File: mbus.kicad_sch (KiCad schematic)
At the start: 30 parts

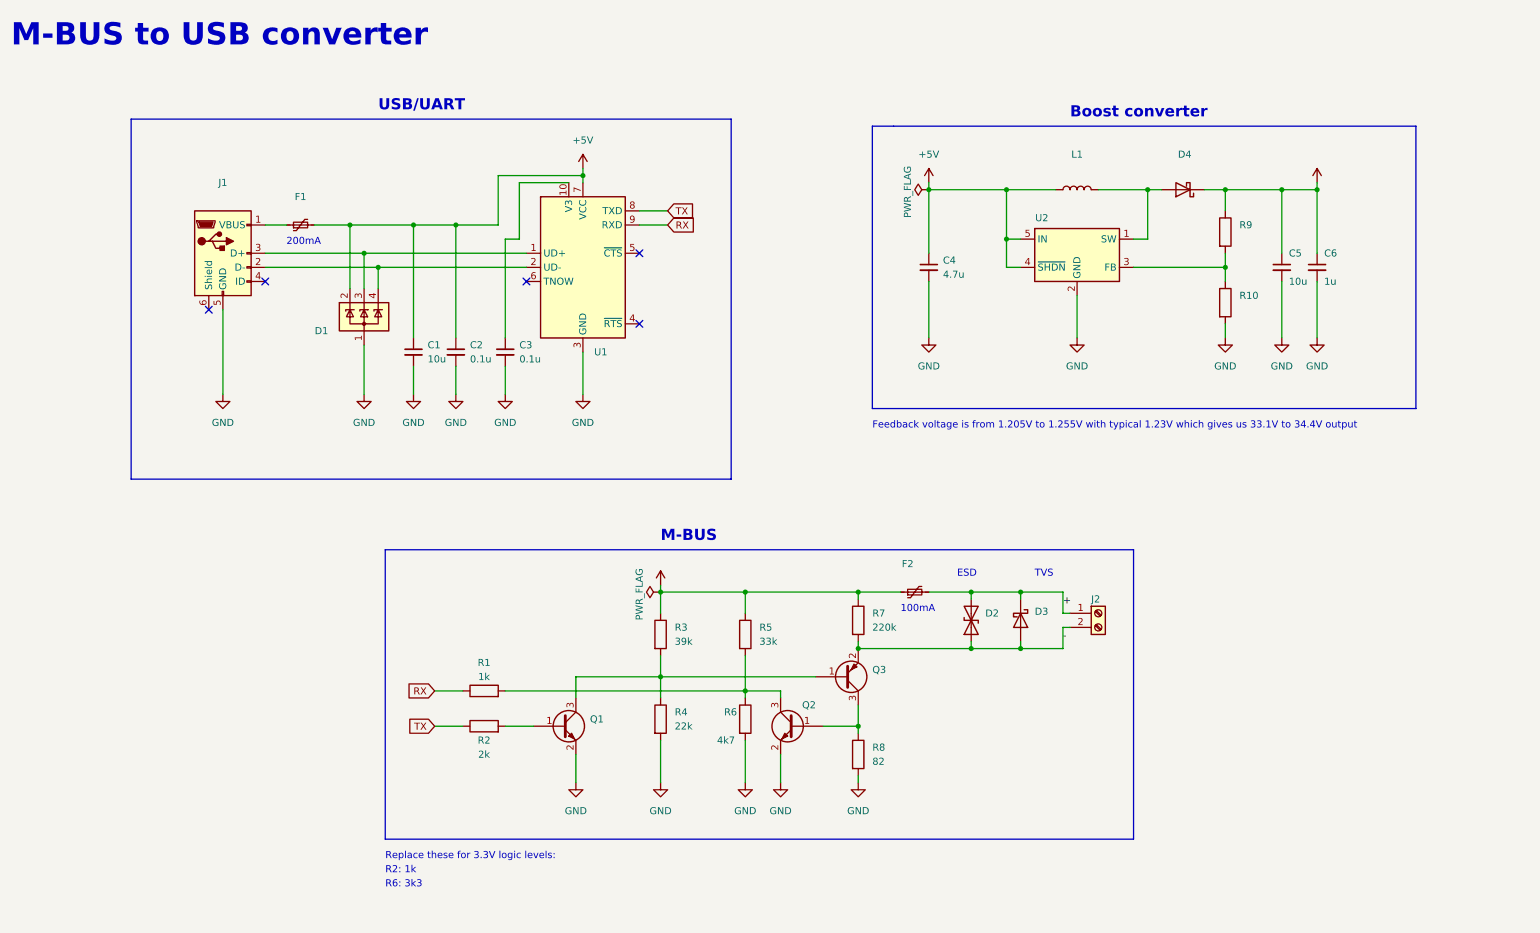
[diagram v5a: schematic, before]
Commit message: Replaced microUSB with type C, changed ESD protection IC
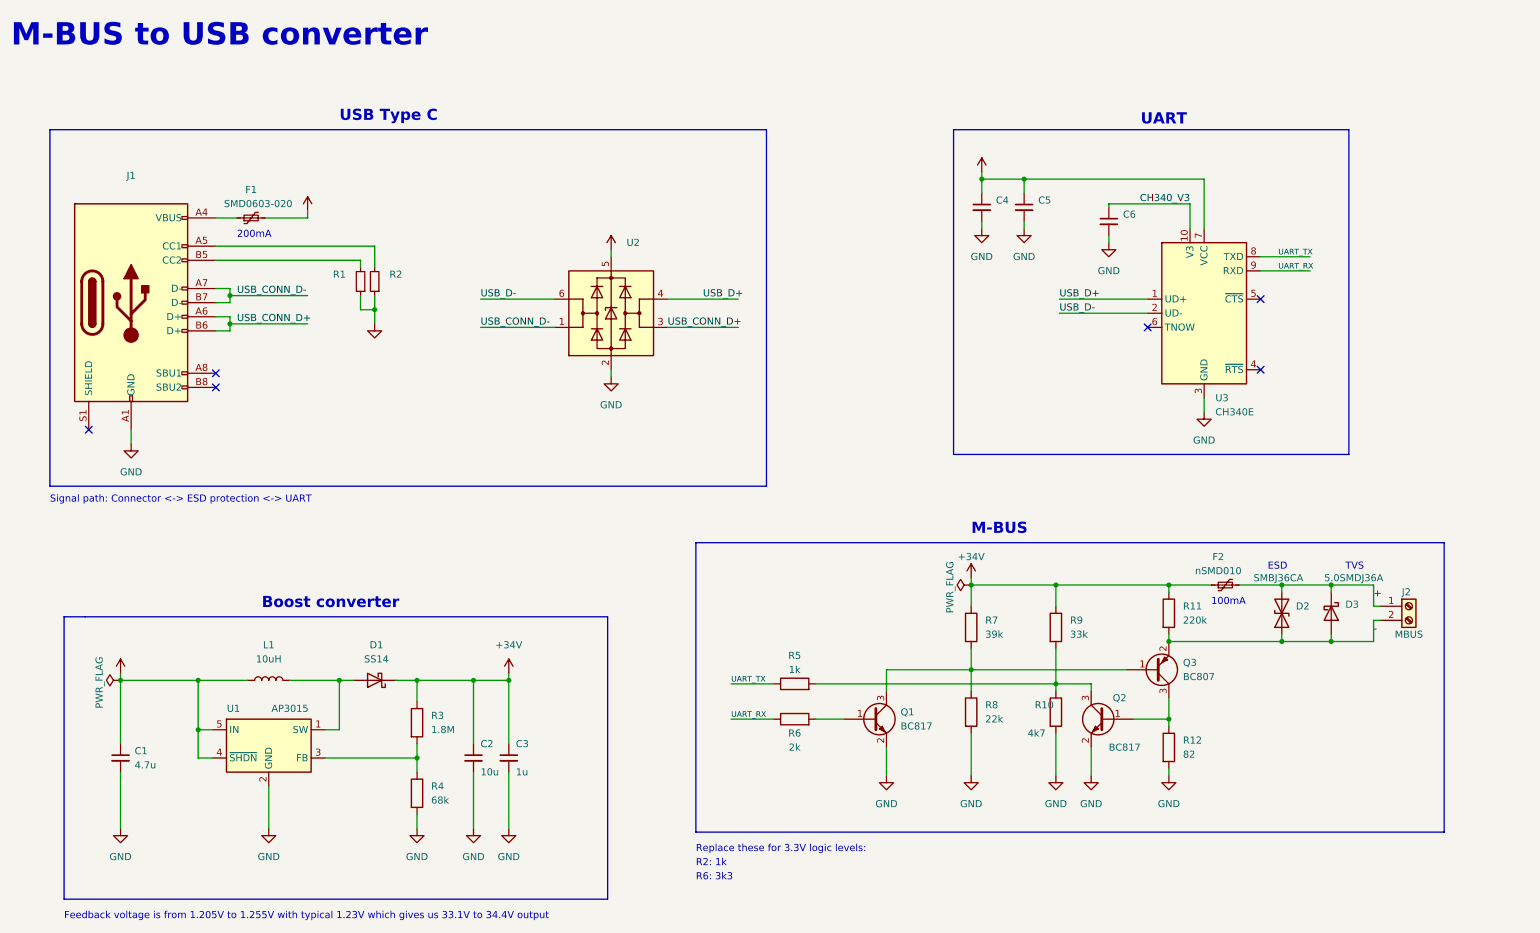
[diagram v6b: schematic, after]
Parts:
- removed D1: (no value), symbol Power_Protection:SP0503BAHT
- removed J1: (no value), symbol Connector:USB_B_Micro
- added J1: (no value), symbol Connector:USB_C_Receptacle_USB2.0
- added R1, R2: (no value), symbol Device:R_Small
- added U2: (no value), symbol Power_Protection:USBLC6-2SC6
- C4: renamed from C1; value 10u -> (none); footprint Capacitor_SMD:C_0603_1608Metric -> (none)
- C5: renamed from C2; value 0.1u -> (none); footprint Capacitor_SMD:C_0603_1608Metric -> (none)
- C6: renamed from C3; value 0.1u -> (none); footprint Capacitor_SMD:C_0603_1608Metric -> (none)
- D1: renamed from D4; value (none) -> SS14; footprint (none) -> Diode_SMD:D_SOD-123F
- D2: value (none) -> SMBJ36CA; footprint (none) -> Diode_SMD:D_SMB
- D3: value (none) -> 5.0SMDJ36A; footprint (none) -> Diode_SMD:D_SMC
- F1: value (none) -> SMD0603-020; footprint (none) -> Fuse:Fuse_0603_1608Metric
- F2: value (none) -> nSMD010; footprint (none) -> Fuse:Fuse_1206_3216Metric
- J2: value (none) -> MBUS; footprint (none) -> TerminalBlock_Phoenix:TerminalBlock_Phoenix_PT-1,5-2-5.0-H_1x02_P5.00mm_Horizontal
- L1: value (none) -> 10uH; footprint (none) -> Inductor_SMD:L_Sunlord_MWSA0518_5.4x5.2mm
- Q1, Q2: value (none) -> BC817; footprint (none) -> Package_TO_SOT_SMD:SOT-23
- Q3: value (none) -> BC807; footprint (none) -> Package_TO_SOT_SMD:SOT-23
- R3: renamed from R9; value (none) -> 1.8M; footprint (none) -> Resistor_SMD:R_0603_1608Metric
- R4: renamed from R10; value (none) -> 68k; footprint (none) -> Resistor_SMD:R_0603_1608Metric
- U1: renamed from U2; value (none) -> AP3015; footprint (none) -> Package_TO_SOT_SMD:SOT-23-5
- U3: renamed from U1; value (none) -> CH340E; footprint (none) -> Package_SO:MSOP-10_3x3mm_P0.5mm
- renumbered C4 to C1, C5 to C2, C6 to C3, R6 to R10, R7 to R11, R8 to R12, R1 to R5, R2 to R6, R3 to R7, R4 to R8, R5 to R9
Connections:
- net GND: now also J1.A1 (GND), J1.A12 (GND), J1.B1 (GND), J1.B12 (GND), R1.1, R2.1, U2.2 (GND)
- net USB_D+: now reaches U3.1 (UD+)
- net USB_D+: now also U2.4 (I/O2)
- net CH340_V3: now reaches C6.1, U3.10 (V3)
- net USB_D-: now reaches U3.2 (UD-)
- net USB_D-: now also U2.6 (I/O1)
- net at F1.1: now also J1.A4 (VBUS), J1.A9 (VBUS), J1.B4 (VBUS), J1.B9 (VBUS)
- net +5V renamed VBUS
- net VBUS: now also U2.5 (VBUS)
- net RX renamed UART_RX
- net UART_RX: now also R6.1; no longer R5.1
- net TX renamed UART_TX
- net UART_TX: now also R5.1; no longer R6.1
- new net: J1.B5 (CC2), R1.2
- new net: J1.A5 (CC1), R2.2
- new net USB_CONN_D+: J1.A6 (D+), J1.B6 (D+), U2.3 (I/O2)
- new net USB_CONN_D-: J1.A7 (D-), J1.B7 (D-), U2.1 (I/O1)
- no-connect marks 5 -> 6
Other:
- note added: "Signal path: Connector <-> ESD protection <-> UART"
- note added: "UART"
- note added: "USB Type C"
- note removed: "USB/UART"
- moved on the sheet: C1, C2, C3, C4, C5, C6, D1, D2, D3, F1, F2, J2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

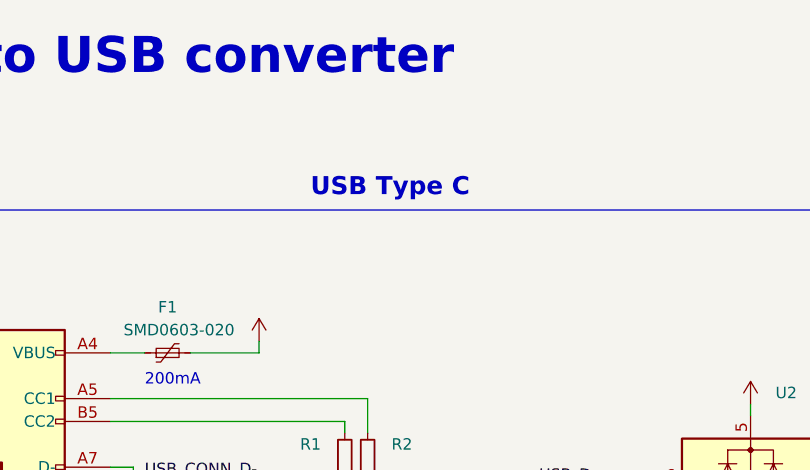
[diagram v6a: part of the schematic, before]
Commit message: Fixed footprint library link, updated exported schematic
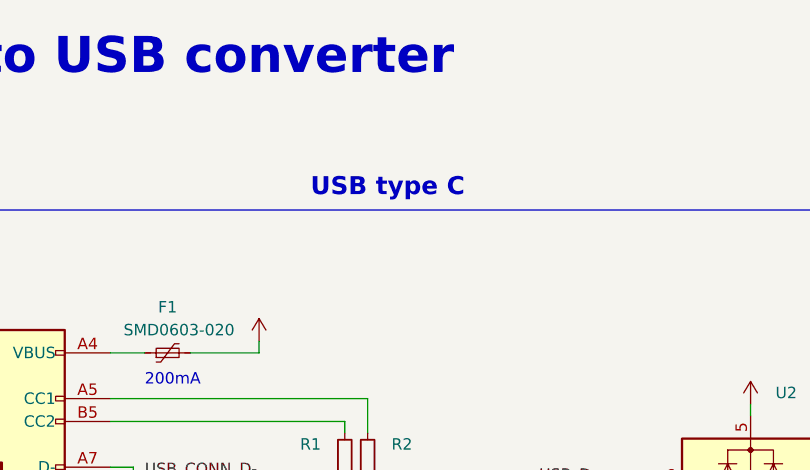
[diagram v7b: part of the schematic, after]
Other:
- note added: "USB type C"
- note removed: "USB Type C"
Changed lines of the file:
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@@
     (effects (font (size 1.27 1.27)) (justify left bottom))
   )
-  (text "USB Type C" (at 73.025 33.655 0)
+  (text "USB type C" (at 73.025 33.655 0)
     (effects (font (size 2 2) (thickness 0.4) bold) (justify left bottom))
   )

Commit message: PCB component placement WIP
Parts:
- C4: value (none) -> 10u; footprint (none) -> Capacitor_SMD:C_0402_1005Metric
- C5, C6: value (none) -> 0.1u; footprint (none) -> Capacitor_SMD:C_0402_1005Metric
- J1: value (none) -> USB_C_Receptacle_USB2.0; footprint (none) -> Connector_USB:USB_C_Receptacle_HRO_TYPE-C-31-M-12
- R1, R2: value (none) -> 5k1; footprint (none) -> Resistor_SMD:R_0402_1005Metric
- U2: value (none) -> USBLC6-2SC6; footprint (none) -> Package_TO_SOT_SMD:SOT-23-6
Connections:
- net USB_CONN_D+: now also U2.1 (I/O1); no longer U2.3 (I/O2)
- net USB_CONN_D-: now also U2.3 (I/O2); no longer U2.1 (I/O1)
- net USB_D+: now also U2.6 (I/O1); no longer U2.4 (I/O2)
- net USB_D-: now also U2.4 (I/O2); no longer U2.6 (I/O1)
- net USB_CC2: now reaches J1.B5 (CC2), R1.2
- net USB_FUSE: now reaches F1.1, J1.A4 (VBUS), J1.A9 (VBUS), J1.B4 (VBUS), J1.B9 (VBUS)
- net USB_CC1: now reaches J1.A5 (CC1), R2.2
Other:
- note added: "R10: 3k3"
- note added: "R6: 1k"
- note removed: "R2: 1k"
- note removed: "R6: 3k3"
- moved on the sheet: F1
